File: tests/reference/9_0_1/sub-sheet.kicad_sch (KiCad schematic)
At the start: 1 part, among them U1 74LS04

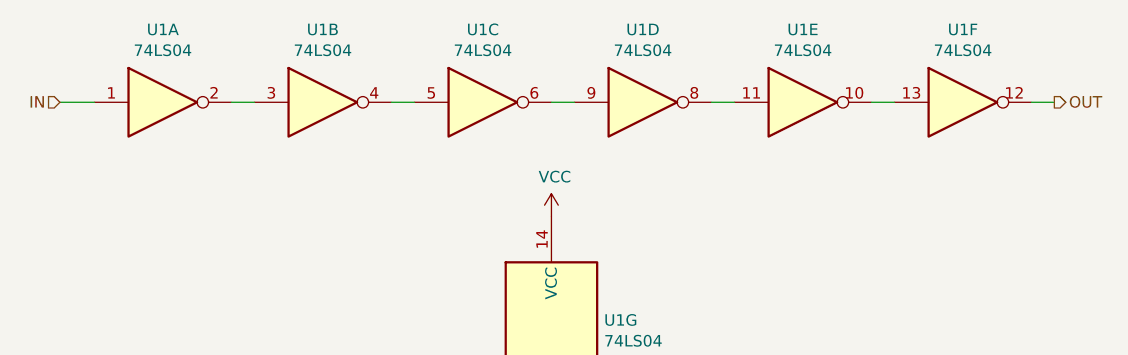
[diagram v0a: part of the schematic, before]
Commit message: [Schematic][Added] Support for private texts on symbols
- Introduced in KiCad 9
- Not documented, as usual
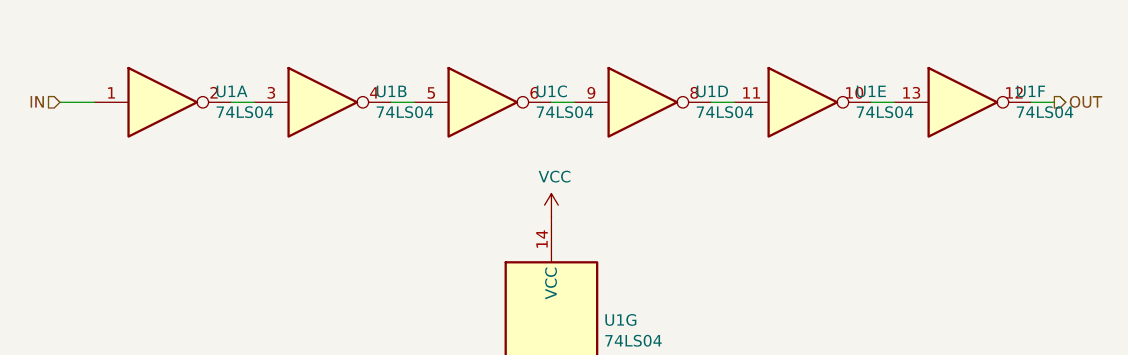
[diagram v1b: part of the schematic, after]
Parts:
- U1: private (none) -> PrivField
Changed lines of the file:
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@@
     (effects (font (size 1.27 1.27)) (justify left))
   )
-  (symbol (lib_id "74xx:74LS04") (at 96.52 63.5 0) (unit 1)
-    (exclude_from_sim no) (in_bom yes) (on_board yes) (dnp no)
-    (property "Reference" "U1" (at 96.52 55.4482 0)
-      (effects (font (size 1.27 1.27)))
-    )
-    (property "Value" "74LS04" (at 96.52 57.7596 0)
-      (effects (font (size 1.27 1.27)))
+  (symbol (lib_name "74LS04_2") (lib_id "74xx:74LS04") (at 96.52 63.5 0) (unit 1)
+    (exclude_from_sim no) (in_bom yes) (on_board yes) (dnp no)
+    (property "Reference" "U1" (at 102.362 62.3316 0)
+      (effects (font (size 1.27 1.27)) (justify left))
+    )
+    (property "Value" "74LS04" (at 102.362 64.643 0)
+      (effects (font (size 1.27 1.27)) (justify left))
     )
     (property "Footprint" "" (at 96.52 63.5 0)
@@
       (effects (font (size 1.27 1.27)) (hide yes))
     )
+    (property private "PrivField" "Testing 1 2 3" (at 96.52 63.5 0)
+      (effects (font (size 1.27 1.27)) (hide yes))
+    )
     (pin "1")
     (pin "2")
@@
     )
   )
-  (symbol (lib_id "74xx:74LS04") (at 114.3 63.5 0) (unit 2)
-    (exclude_from_sim no) (in_bom yes) (on_board yes) (dnp no)
-    (property "Reference" "U1" (at 114.3 55.4482 0)
-      (effects (font (size 1.27 1.27)))
-    )
-    (property "Value" "74LS04" (at 114.3 57.7596 0)
-      (effects (font (size 1.27 1.27)))
+  (symbol (lib_name "74LS04_1") (lib_id "74xx:74LS04") (at 114.3 63.5 0) (unit 2)
+    (exclude_from_sim no) (in_bom yes) (on_board yes) (dnp no)
+    (property "Reference" "U1" (at 120.142 62.3316 0)
+      (effects (font (size 1.27 1.27)) (justify left))
+    )
+    (property "Value" "74LS04" (at 120.142 64.643 0)
+      (effects (font (size 1.27 1.27)) (justify left))
     )
     (property "Footprint" "" (at 114.3 63.5 0)
@@
       (effects (font (size 1.27 1.27)) (hide yes))
     )
+    (property private "PrivField" "Testing 1 2 3" (at 114.3 63.5 0)
+      (effects (font (size 1.27 1.27)) (hide yes))
+    )
     (pin "1")
     (pin "2")
@@
     )
   )
-  (symbol (lib_id "74xx:74LS04") (at 132.08 63.5 0) (unit 3)
-    (exclude_from_sim no) (in_bom yes) (on_board yes) (dnp no)
-    (property "Reference" "U1" (at 132.08 55.4482 0)
-      (effects (font (size 1.27 1.27)))
-    )
-    (property "Value" "74LS04" (at 132.08 57.7596 0)
-      (effects (font (size 1.27 1.27)))
+  (symbol (lib_name "74LS04_6") (lib_id "74xx:74LS04") (at 132.08 63.5 0) (unit 3)
+    (exclude_from_sim no) (in_bom yes) (on_board yes) (dnp no)
+    (property "Reference" "U1" (at 137.922 62.3316 0)
+      (effects (font (size 1.27 1.27)) (justify left))
+    )
+    (property "Value" "74LS04" (at 137.922 64.643 0)
+      (effects (font (size 1.27 1.27)) (justify left))
     )
     (property "Footprint" "" (at 132.08 63.5 0)
@@
       (effects (font (size 1.27 1.27)) (hide yes))
     )
+    (property private "PrivField" "Testing 1 2 3" (at 132.08 63.5 0)
+      (effects (font (size 1.27 1.27)) (hide yes))
+    )
     (pin "1")
     (pin "2")
@@
     )
   )
-  (symbol (lib_id "74xx:74LS04") (at 149.86 63.5 0) (unit 4)
-    (exclude_from_sim no) (in_bom yes) (on_board yes) (dnp no)
-    (property "Reference" "U1" (at 149.86 55.4482 0)
-      (effects (font (size 1.27 1.27)))
-    )
-    (property "Value" "74LS04" (at 149.86 57.7596 0)
-      (effects (font (size 1.27 1.27)))
+  (symbol (lib_name "74LS04_5") (lib_id "74xx:74LS04") (at 149.86 63.5 0) (unit 4)
+    (exclude_from_sim no) (in_bom yes) (on_board yes) (dnp no)
+    (property "Reference" "U1" (at 155.702 62.3316 0)
+      (effects (font (size 1.27 1.27)) (justify left))
+    )
+    (property "Value" "74LS04" (at 155.702 64.643 0)
+      (effects (font (size 1.27 1.27)) (justify left))
     )
     (property "Footprint" "" (at 149.86 63.5 0)
@@
       (effects (font (size 1.27 1.27)) (hide yes))
     )
+    (property private "PrivField" "Testing 1 2 3" (at 149.86 63.5 0)
+      (effects (font (size 1.27 1.27)) (hide yes))
+    )
     (pin "1")
     (pin "2")
@@
     )
   )
-  (symbol (lib_id "74xx:74LS04") (at 167.64 63.5 0) (unit 5)
-    (exclude_from_sim no) (in_bom yes) (on_board yes) (dnp no)
-    (property "Reference" "U1" (at 167.64 55.4482 0)
-      (effects (font (size 1.27 1.27)))
-    )
-    (property "Value" "74LS04" (at 167.64 57.7596 0)
-      (effects (font (size 1.27 1.27)))
+  (symbol (lib_name "74LS04_3") (lib_id "74xx:74LS04") (at 167.64 63.5 0) (unit 5)
+    (exclude_from_sim no) (in_bom yes) (on_board yes) (dnp no)
+    (property "Reference" "U1" (at 173.482 62.3316 0)
+      (effects (font (size 1.27 1.27)) (justify left))
+    )
+    (property "Value" "74LS04" (at 173.482 64.643 0)
+      (effects (font (size 1.27 1.27)) (justify left))
     )
     (property "Footprint" "" (at 167.64 63.5 0)
@@
       (effects (font (size 1.27 1.27)) (hide yes))
     )
+    (property private "PrivField" "Testing 1 2 3" (at 167.64 63.5 0)
+      (effects (font (size 1.27 1.27)) (hide yes))
+    )
     (pin "1")
     (pin "2")
@@
     )
   )
-  (symbol (lib_id "74xx:74LS04") (at 185.42 63.5 0) (unit 6)
-    (exclude_from_sim no) (in_bom yes) (on_board yes) (dnp no)
-    (property "Reference" "U1" (at 185.42 55.4482 0)
-      (effects (font (size 1.27 1.27)))
-    )
-    (property "Value" "74LS04" (at 185.42 57.7596 0)
-      (effects (font (size 1.27 1.27)))
+  (symbol (lib_name "74LS04_4") (lib_id "74xx:74LS04") (at 185.42 63.5 0) (unit 6)
+    (exclude_from_sim no) (in_bom yes) (on_board yes) (dnp no)
+    (property "Reference" "U1" (at 191.262 62.3316 0)
+      (effects (font (size 1.27 1.27)) (justify left))
+    )
+    (property "Value" "74LS04" (at 191.262 64.643 0)
+      (effects (font (size 1.27 1.27)) (justify left))
     )
     (property "Footprint" "" (at 185.42 63.5 0)
@@
       (effects (font (size 1.27 1.27)) (hide yes))
     )
+    (property private "PrivField" "Testing 1 2 3" (at 185.42 63.5 0)
+      (effects (font (size 1.27 1.27)) (hide yes))
+    )
     (pin "1")
     (pin "2")
@@
       (effects (font (size 1.27 1.27)) (hide yes))
     )
+    (property private "PrivField" "Testing 1 2 3" (at 139.7 88.9 0)
+      (effects (font (size 1.27 1.27)) (hide yes))
+    )
